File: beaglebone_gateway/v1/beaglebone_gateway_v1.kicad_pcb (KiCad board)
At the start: 2 copper layers, 86.4 x 54.6 mm, 35 parts, among them J1 PWR_CONNECTOR, J2 BATT CURENT SENSING, J3 EXT_I2C, J4 EXT_UART, P8 BeagleBone_Black_Header, P9 BeagleBone_Black_Header, U1 RA-02_LORA, U2 ACS725xLCTR-10AU, U3 BME280, U4 R-78B5.0-2.0

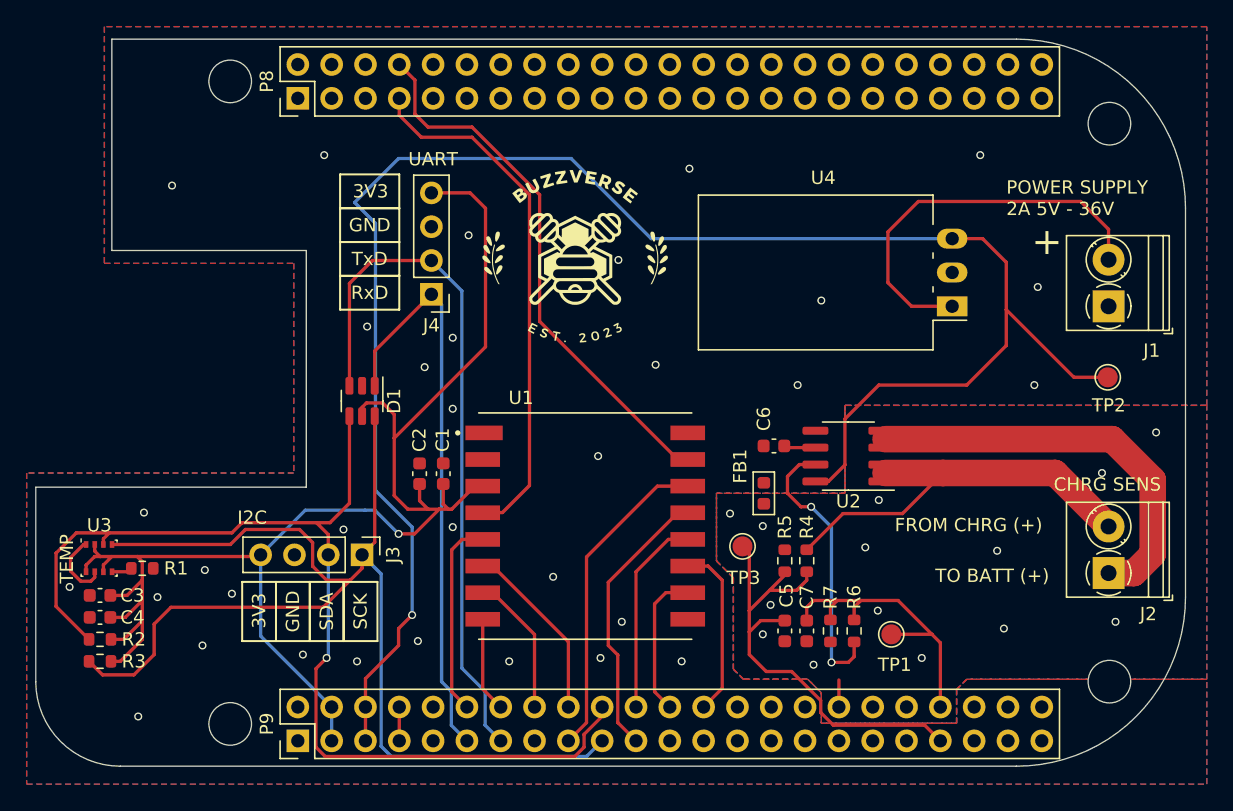
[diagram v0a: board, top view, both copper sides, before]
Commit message: Add ADC divider cut off using complementary mosfet transistors
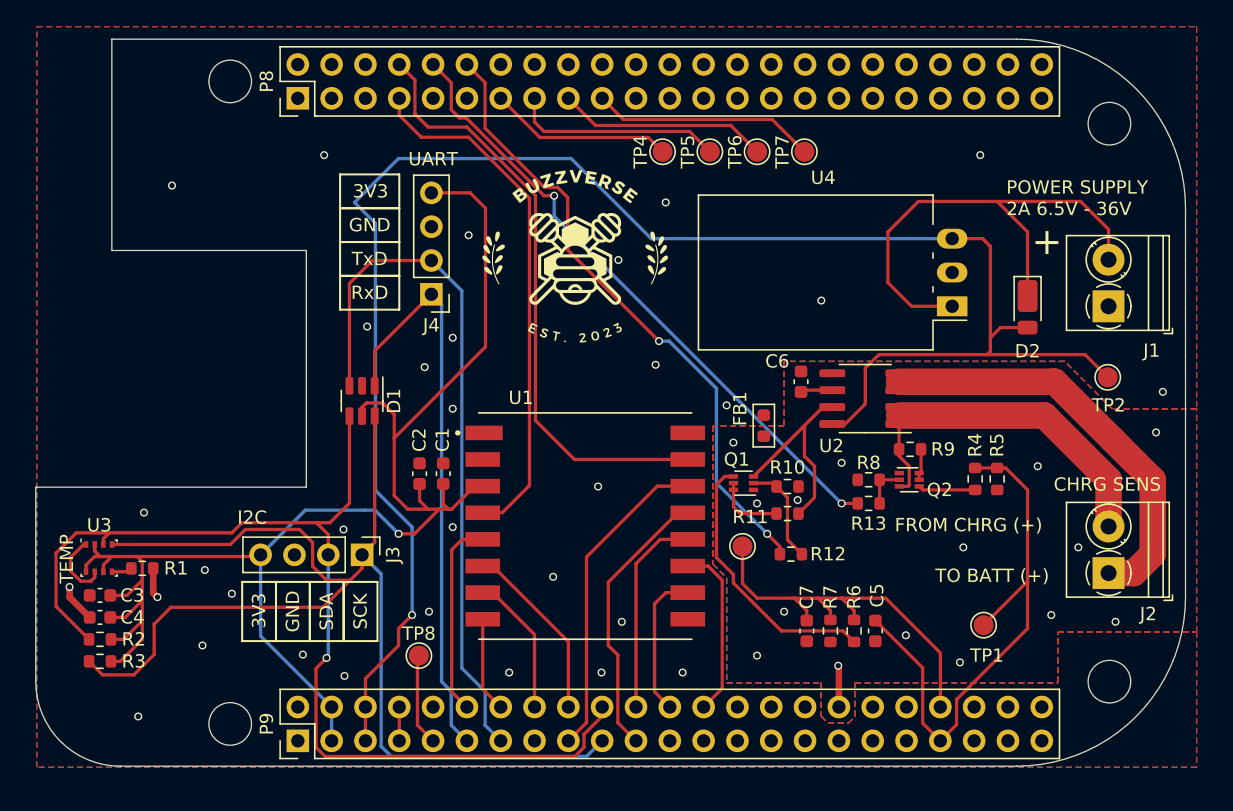
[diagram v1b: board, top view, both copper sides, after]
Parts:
- added D2: SBR3U60P1Q-7, Diode_SMD:D_PowerDI-123, F.Cu at (174.5, 65.5)
- added Q1: DMC2400UV, Package_TO_SOT_SMD:SOT-563, F.Cu at (153.2, 78.7)
- added Q2: DMC2400UV, Package_TO_SOT_SMD:SOT-563, F.Cu at (165.6, 78.5)
- added R10: 1M, Resistor_SMD:R_0603_1608Metric, F.Cu at (156.5, 79.0)
- added R11: 1M, Resistor_SMD:R_0603_1608Metric, F.Cu at (156.5, 81.0)
- added R12: 100, Resistor_SMD:R_0603_1608Metric, F.Cu at (156.7, 84.1)
- added R13: 100, Resistor_SMD:R_0603_1608Metric, F.Cu at (162.6, 80.3)
- added R8: 1M, Resistor_SMD:R_0603_1608Metric, F.Cu at (162.6, 78.5)
- added R9: 1M, Resistor_SMD:R_0603_1608Metric, F.Cu at (165.7, 76.2)
- added TP4: GPIO23, TestPoint:TestPoint_Pad_D1.5mm, F.Cu at (147.1, 53.8)
- added TP5: GPIO47, TestPoint:TestPoint_Pad_D1.5mm, F.Cu at (150.6, 53.8)
- added TP6: GPIO27, TestPoint:TestPoint_Pad_D1.5mm, F.Cu at (154.2, 53.8)
- added TP7: GPIO22, TestPoint:TestPoint_Pad_D1.5mm, F.Cu at (157.7, 53.8)
- added TP8: PWR_BUT, TestPoint:TestPoint_Pad_D1.5mm, F.Cu at (128.8, 91.7)
- C1: value 22uF -> 100n
- C2: value 0.1uF -> 100n
- R2, R3: value 10k -> 4.7k
- TP1: value Charge_current_test -> Batt_voltage
- TP3: value Batt_voltage -> Charge_current_test
- U4: value R-78B5.0-2.0 -> R-78K5.0-2.0
- moved R5 17.1 mm to (172.2, 78.4), turned to -90 degrees
- moved R4 14.1 mm to (170.6, 78.4), turned to 90 degrees
- moved TP1 6.97 mm to (171.2, 89.4)
- moved C5 6.81 mm to (163.1, 89.8)
- moved C6 5.24 mm to (157.5, 71.1), turned to 90 degrees
- moved FB1 5.08 mm to (154.7, 74.4)
- moved U2 4.50 mm to (162.3, 72.4)
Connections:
- C6 pad 2: GNDD -> GNDA
- P8 pad 10: /GPIO68 -> BATT_VOLTAGE_ADC_EN
- P8 pad 12: /GPIO44 -> BATT_CHARGE_CURRENT_ADC_EN
- R4 pad 1: Net-(J2-Pin_2) -> Net-(Q2B-S2)
- R6 pad 1: Net-(U2-VIOUT) -> Net-(Q1B-S2)
- TP1 pad 1: CHARGE_CURRENT_SENSING -> BATT_VOLTAGE_ANALOG
- TP3 pad 1: BATT_VOLTAGE_ANALOG -> CHARGE_CURRENT_SENSING
- U2 pad 5: GNDD -> GNDA
- U2 pad 7: Net-(U2-VIOUT) -> Net-(Q1B-D2)
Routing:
- net BATT_VOLTAGE_ADC_EN: track 0.00 -> 47.6 mm, vias 0 -> 2
- net BATT_CHARGE_CURRENT_ADC_EN: track 0.00 -> 47.6 mm, vias 0 -> 2
- net Net-(U2-VIOUT): track 21.2 -> 0.00 mm, vias 2 -> 0
- net Net-(Q1B-S2): track 0.00 -> 20.3 mm
- net /GPIO22: track 0.00 -> 16.9 mm
- net /GPIO47: track 0.00 -> 15.9 mm
- net /GPIO27: track 0.00 -> 15.8 mm
- net Net-(Q1B-D2): track 0.00 -> 15.6 mm
- net /GPIO23: track 0.00 -> 13.8 mm
- net Net-(D2-K): track 30.0 -> 38.1 mm
- net Net-(Q1A-G1): track 0.00 -> 7.70 mm
- net /PWR_BUT: track 0.00 -> 6.93 mm
- net CHARGE_CURRENT_SENSING: track 23.8 -> 30.0 mm
- net Net-(Q1A-D1): track 0.00 -> 5.22 mm
- net BATT_VOLTAGE_ANALOG: track 36.7 -> 41.9 mm
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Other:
- board text added: "POWER SUPPLY 2A 6.5V - 36V"
- board text removed: "POWER SUPPLY 2A 5V - 36V"
